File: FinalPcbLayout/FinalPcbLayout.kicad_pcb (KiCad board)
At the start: 4 copper layers, 106.7 x 78.7 mm, 52 parts, among them J1 Conn_02x05_Odd_Even, J2 Conn_01x04_Pin, J3 Serial Out, J4 Conn_01x11_Pin, J5 USB_C_Receptacle, J6 Conn_01x02_Pin, J8 Micro_SD_Card, Q1 NMOS, SW1 SW_Push, U1 ESP32-WROOM-32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

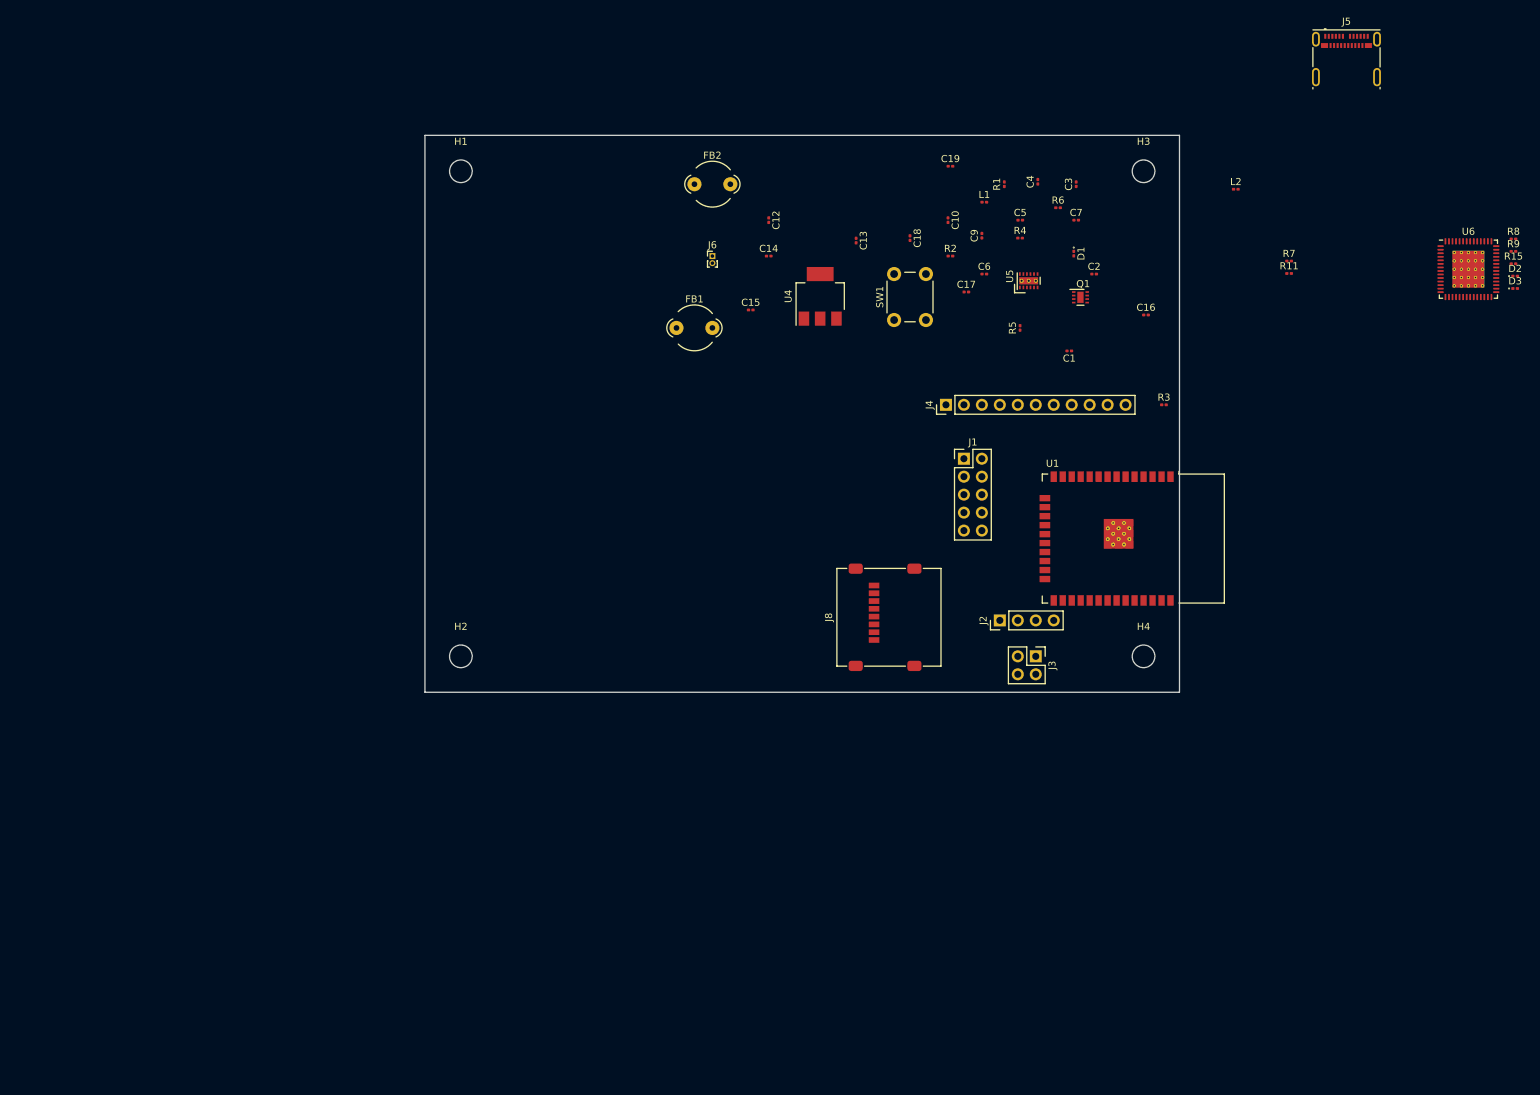
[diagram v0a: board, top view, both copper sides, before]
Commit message: route some gnd
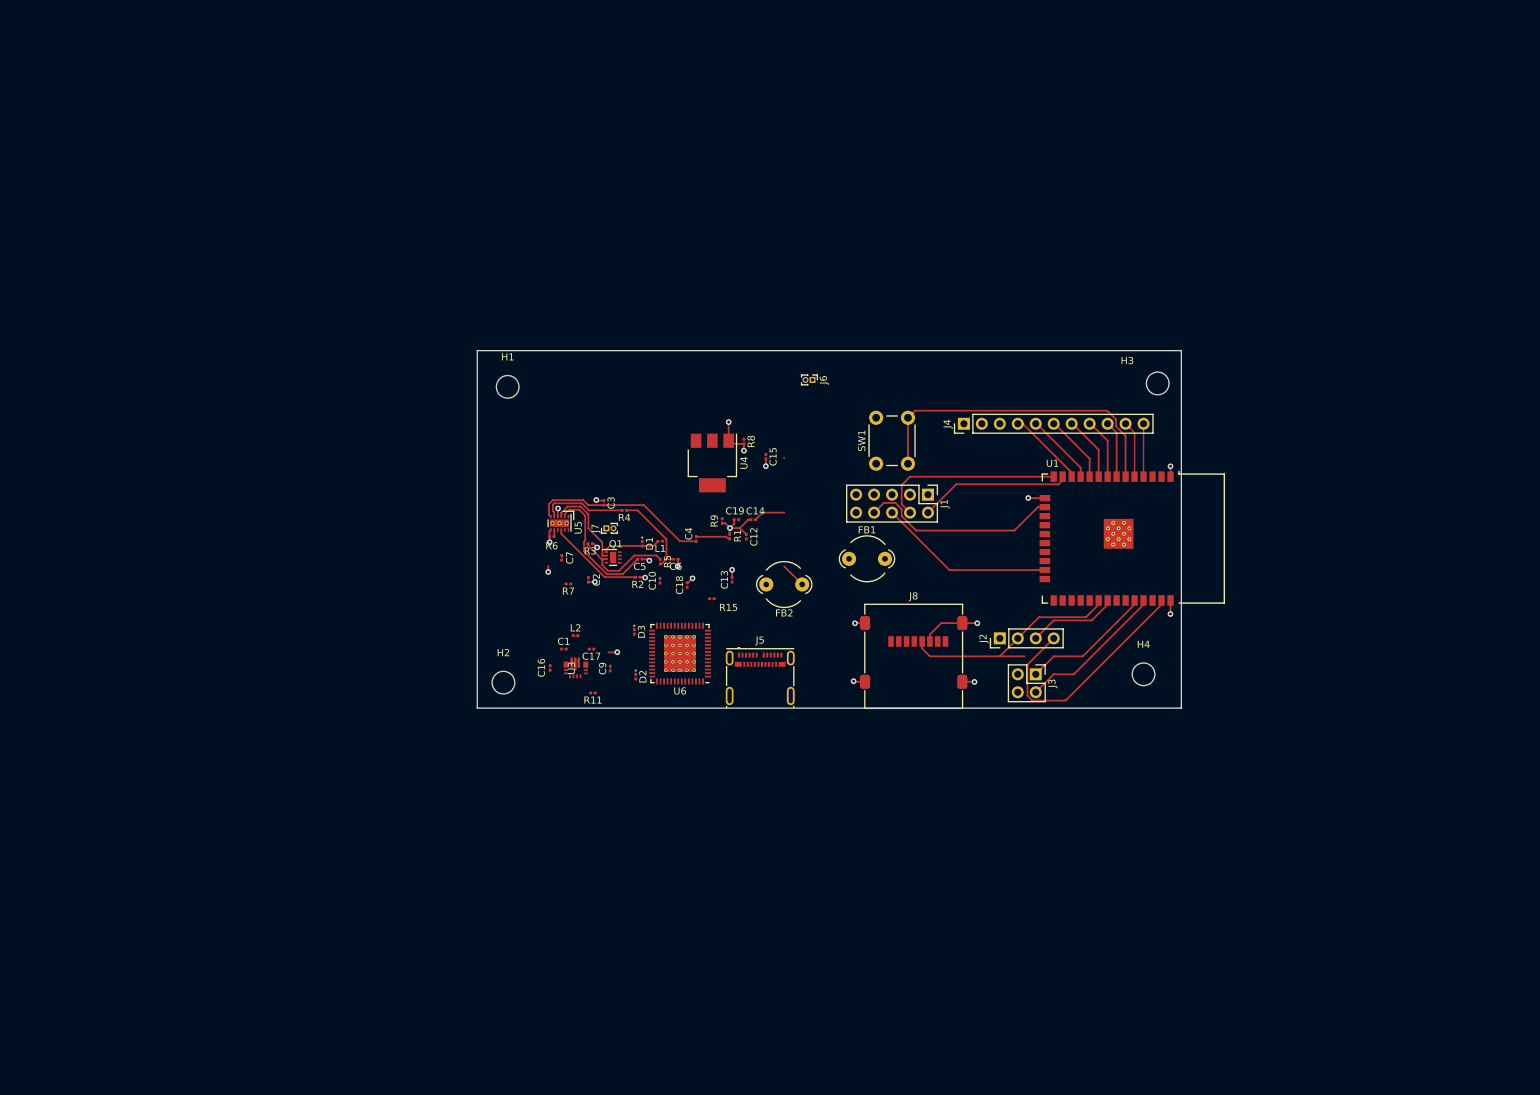
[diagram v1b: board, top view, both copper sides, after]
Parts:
- added J7: Conn_01x02_Pin, Connector_PinHeader_1.00mm:PinHeader_1x02_P1.00mm_Vertical, F.Cu at (101.8, 101.3)
- added U3: ~, OSMI-parts:VQFN-15-1EP-2.5x3mm_P0.5mm, F.Cu at (97.5, 121.0)
- moved D2 136.6 mm to (106.0, 122.3), turned to -90 degrees
- moved D3 133.7 mm to (105.8, 115.9), turned to -90 degrees
- moved U6 124.0 mm to (112.3, 119.0), turned to 180 degrees
- moved R15 122.8 mm to (116.8, 111.2)
- moved J5 120.5 mm to (123.6, 122.4)
- moved R9 118.2 mm to (118.2, 100.2), turned to -90 degrees
- moved R11 114.9 mm to (100.0, 124.5), turned to 180 degrees
- moved L2 112.7 mm to (97.5, 116.5)
- moved R8 112.5 mm to (121.3, 89.0), turned to -90 degrees
- moved R7 111.6 mm to (96.5, 109.1), turned to 180 degrees
- moved C16 97.9 mm to (93.9, 121.0), turned to -90 degrees
- moved C7 87.0 mm to (95.5, 105.5), turned to 90 degrees
- moved R6 85.4 mm to (94.1, 102.5)
- moved C2 83.6 mm to (99.3, 108.6), turned to 90 degrees
- moved R3 83.5 mm to (99.6, 103.5), turned to 180 degrees
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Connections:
- J5 pad A1: /usb/GND1 -> GND
- J5 pad A12: /usb/GND1 -> GND
- J5 pad A5: Net-(J5-CC1) -> /usb/PD1_CC1
- J5 pad A6: /usb/D+1 -> /usb/D+
- J5 pad A7: /usb/D-1 -> /usb/D-
- J5 pad B1: /usb/GND1 -> GND
- J5 pad B12: /usb/GND1 -> GND
- J5 pad B5: Net-(J5-CC2) -> /usb/PD1_CC2
- J5 pad B6: /usb/D-1 -> /usb/D+
- J5 pad B7: /usb/D+1 -> /usb/D-
- U6 pad 11: unconnected-(U6-VCORE-Pad11) -> +1V2
- U6 pad 19: unconnected-(U6-VREGOUT-Pad19) -> +1V2
- U6 pad 22: unconnected-(U6-VCORE-Pad22) -> +1V2
- U6 pad 36: unconnected-(U6-VCORE-Pad36) -> +1V2
- U6 pad 46: unconnected-(U6-VCORE-Pad46) -> +1V2
- U6 pad 52: unconnected-(U6-PD1_CC2-Pad52) -> /usb/PD1_CC2
- U6 pad 55: unconnected-(U6-PD1_CC1-Pad55) -> /usb/PD1_CC1
- U6 pad 56: unconnected-(U6-VCORE-Pad56) -> +1V2
- U6 pad 7: unconnected-(U6-GPIO0-Pad7) -> /usb/I2CSDA
- U6 pad 8: unconnected-(U6-GPIO1-Pad8) -> /usb/I2CSCL
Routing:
- net GND: track 0.00 -> 48.2 mm, vias 0 -> 23
- net /ESTOP: track 0.00 -> 45.5 mm
- net /COPI: track 0.00 -> 35.1 mm
- net /SCLK: track 0.00 -> 33.5 mm
- net /JTAG_TDI: track 0.00 -> 28.3 mm
- net /JTAG_TCK: track 0.00 -> 26.4 mm
- net Net-(U5-COMP): track 0.00 -> 25.3 mm
- net /JTAG_TDO: track 0.00 -> 25.0 mm
- net /JTAG_TMS: track 0.00 -> 21.4 mm
- net Net-(J3-Pin_2): track 0.00 -> 21.0 mm
- net Net-(U5-VCC): track 0.00 -> 18.7 mm
- net Net-(J3-Pin_1): track 0.00 -> 18.6 mm
- net Net-(Q1-S): track 0.00 -> 14.1 mm
- net Net-(U5-RT): track 0.00 -> 13.6 mm
- net /CIPO: track 0.00 -> 12.7 mm
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- added copper zone on In1.Cu, net GND
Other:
- board size 106.7 x 78.7 mm -> 99.5 x 50.5 mm

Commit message: power supplies
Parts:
- removed J1: Conn_02x05_Odd_Even, Connector_PinHeader_2.54mm:PinHeader_2x05_P2.54mm_Vertical
- removed J3: Serial Out, Connector_PinHeader_2.54mm:PinHeader_2x02_P2.54mm_Vertical
- removed R9: 5.1k, Resistor_SMD:R_0201_0603Metric
- added C11: 22uF, Capacitor_SMD:C_0603_1608Metric, F.Cu at (65.3, 105.0)
- added C20: 3.3u, Capacitor_SMD:C_0603_1608Metric, F.Cu at (59.3, 102.5)
- added C8: 1uF, Capacitor_SMD:C_0603_1608Metric, F.Cu at (65.3, 102.5)
- added R10: 523k, Resistor_SMD:R_0603_1608Metric, F.Cu at (137.2, 95.2)
- added R12: 100k, Resistor_SMD:R_0603_1608Metric, F.Cu at (137.2, 96.8)
- added R13: 10k, Resistor_SMD:R_0603_1608Metric, F.Cu at (128.7, 96.6)
- added R14: 10k 1%, Resistor_SMD:R_0603_1608Metric, F.Cu at (59.3, 105.0)
- added R16: 1k, Resistor_SMD:R_0603_1608Metric, F.Cu at (59.3, 107.5)
- added R17: 1k, Resistor_SMD:R_0603_1608Metric, F.Cu at (59.3, 110.0)
- added R18: ???, Resistor_SMD:R_0603_1608Metric, F.Cu at (59.3, 112.5)
- added R19: ???, Resistor_SMD:R_0603_1608Metric, F.Cu at (59.3, 115.0)
- added U2: ~, Package_DFN_QFN:QFN-16-1EP_3x3mm_P0.5mm_EP1.45x1.45mm, F.Cu at (154.8, 100.2)
- C1, C10, C16, C17, C18, C19, C2, C3, C4, C5, C6, C7, C9: footprint Capacitor_SMD:C_0201_0603Metric -> Capacitor_SMD:C_0603_1608Metric
- C12, C13, C14, C15: footprint Resistor_SMD:R_0201_0603Metric -> Capacitor_SMD:C_0603_1608Metric
- D1: footprint Diode_SMD:D_0201_0603Metric -> Diode_SMD:D_0603_1608Metric
- J2: footprint Connector_PinHeader_2.54mm:PinHeader_1x04_P2.54mm_Vertical -> TerminalBlock_TE-Connectivity:TerminalBlock_TE_282834-4_1x04_P2.54mm_Horizontal
- J6: footprint Connector_PinHeader_1.00mm:PinHeader_1x02_P1.00mm_Vertical -> Connector_PinHeader_2.54mm:PinHeader_1x02_P2.54mm_Horizontal
- L1, L2: footprint Inductor_SMD:L_0201_0603Metric -> Inductor_SMD:L_Coilcraft_XAL8050-223
- R1, R11, R15, R2, R3, R4, R5, R6, R7: footprint Resistor_SMD:R_0201_0603Metric -> Resistor_SMD:R_0603_1608Metric
- R8: value 5.1k -> 370k; footprint Resistor_SMD:R_0201_0603Metric -> Resistor_SMD:R_0603_1608Metric
- SW1: footprint Button_Switch_THT:SW_PUSH_6mm -> TerminalBlock_TE-Connectivity:TerminalBlock_TE_282834-2_1x02_P2.54mm_Horizontal
- U4: footprint Package_TO_SOT_SMD:SOT-223-3_TabPin2 -> Package_TO_SOT_SMD:SOT-223
- moved J4 71.9 mm to (86.0, 114.0), turned to 180 degrees
- moved C10 54.1 mm to (112.7, 162.7)
- moved D2 54.1 mm to (109.2, 176.2)
- moved J7 54.1 mm to (105.1, 155.2)
- moved R2 54.1 mm to (109.5, 162.1)
- moved C7 54.1 mm to (98.8, 159.4)
- moved D3 54.1 mm to (109.0, 169.9)
- moved R15 54.1 mm to (120.0, 165.2)
- moved R3 54.1 mm to (102.8, 157.4)
- moved C6 54.1 mm to (114.9, 159.6)
- moved Q1 54.1 mm to (106.0, 159.4)
- moved R5 54.1 mm to (112.7, 159.9)
- moved U6 54.1 mm to (115.5, 172.9)
- moved H2 52.6 mm to (72.4, 173.5)
- moved C9 47.8 mm to (133.8, 157.2)
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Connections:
- R8 pad 1: Net-(J5-CC2) -> +5V
- R8 pad 2: GND -> /SD_MODE
- U1 pad 34: Net-(J3-Pin_1) -> unconnected-(U1-RXD0/IO3-Pad34)
- U1 pad 35: Net-(J3-Pin_2) -> unconnected-(U1-TXD0/IO1-Pad35)
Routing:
- net +3.3V: track 0.00 -> 35.0 mm
- net /ESTOP: track 45.5 -> 13.0 mm, vias 0 -> 1
- net /JTAG_TDI: track 28.3 -> 0.00 mm
- net /IO22: track 0.00 -> 28.2 mm, vias 0 -> 2
- net /IO17: track 0.00 -> 27.9 mm
- net /JTAG_TCK: track 26.4 -> 0.00 mm
- net /JTAG_TDO: track 25.0 -> 0.00 mm
- net /JTAG_TMS: track 21.4 -> 0.00 mm
- net Net-(J3-Pin_2): track 21.0 -> 0.00 mm
- net /COPI: track 35.1 -> 14.7 mm, vias 0 -> 1
- net Net-(U5-COMP): track 25.3 -> 5.75 mm
- net Net-(J3-Pin_1): track 18.6 -> 0.00 mm
- net GND: track 48.2 -> 30.2 mm, vias 23 -> 22
- net /SCLK: track 33.5 -> 49.8 mm
- net Net-(U3-L2): track 0.00 -> 16.0 mm, vias 0 -> 11
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- added copper zone on F.Cu, net +5V
- added copper zone on In2.Cu, net +5V
- added copper zone on F.Cu, net /Power/USB_Vin
- added copper zone on F.Cu, net GND
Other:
- board size 99.5 x 50.5 mm -> 99.5 x 46.2 mm

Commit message: pOWER DONE
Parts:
- removed J7: Conn_01x02_Pin, Connector_PinHeader_1.00mm:PinHeader_1x02_P1.00mm_Vertical
- C5: value C -> 1uF
- D1: footprint Diode_SMD:D_0603_1608Metric -> SL42_E3_57T:CR_2-E3&slash_57T_VIS
- moved C10 93.4 mm to (168.8, 88.0), turned to 0 degrees
- moved C20 75.2 mm to (132.3, 120.6)
- moved R14 75.2 mm to (132.3, 123.1)
- moved R16 75.2 mm to (132.3, 125.6)
- moved R17 75.2 mm to (132.3, 128.1)
- moved R18 75.2 mm to (132.3, 130.6)
- moved R19 75.2 mm to (132.3, 133.1)
- moved C11 75.2 mm to (138.3, 123.1)
- moved R2 69.1 mm to (102.5, 93.4), turned to -90 degrees
- moved D2 64.4 mm to (127.1, 114.4)
- moved D3 64.4 mm to (126.9, 108.0)
- moved U6 64.4 mm to (133.4, 111.1)
- moved R15 58.5 mm to (141.1, 110.6)
- moved C9 54.2 mm to (96.2, 118.0), turned to 180 degrees
- moved C6 52.9 mm to (108.4, 107.1)
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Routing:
- net +5V: track 14.6 -> 36.4 mm
- net Net-(Q1-G): track 0.00 -> 20.2 mm, vias 0 -> 2
- net Net-(D1-A): track 0.00 -> 12.3 mm
- net +12V: track 0.00 -> 11.3 mm, vias 0 -> 2
- net Net-(U5-CS): track 0.00 -> 10.6 mm
- net Net-(Q1-S): track 0.00 -> 10.0 mm
- net GND: track 30.2 -> 36.7 mm, vias 22 -> 29
- net Net-(U5-RT): track 0.00 -> 2.46 mm
- net Net-(U5-SS): track 0.00 -> 2.30 mm
- net Net-(C6-Pad2): track 1.19 -> 2.98 mm
- added copper zone on F.Cu, net +12V

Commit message: Tyra's work is done here
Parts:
- removed C20: 3.3u, Capacitor_SMD:C_0603_1608Metric
- removed D2, D3: LED, LED_SMD:LED_0201_0603Metric
- removed J5: USB_C_Receptacle, Connector_USB:USB_C_Receptacle_Molex_105450-0101
- removed R14, R15: 10k 1%, Resistor_SMD:R_0603_1608Metric
- removed R16, R17: 1k, Resistor_SMD:R_0603_1608Metric
- removed R18, R19: ???, Resistor_SMD:R_0603_1608Metric
- removed U6: ~, Package_DFN_QFN:QFN-56-1EP_8x8mm_P0.5mm_EP4.5x5.2mm_ThermalVias
- moved C11 40.8 mm to (163.1, 90.7), turned to 180 degrees
- moved J4 1.50 mm to (84.2, 116.4)
- moved H3 1.40 mm to (179.3, 83.4)
- moved SW1 1.30 mm to (173.4, 83.5)
- moved C14 0.52 mm to (158.6, 116.0)
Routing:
- net /IO33: track 0.00 -> 102.8 mm, vias 0 -> 1
- net /IO35: track 0.00 -> 102.5 mm, vias 0 -> 2
- net /IO25: track 0.00 -> 102.2 mm, vias 0 -> 1
- net /IO27: track 0.00 -> 102.0 mm, vias 0 -> 2
- net /IO26: track 0.00 -> 101.1 mm, vias 0 -> 2
- net /Sense_VN: track 0.00 -> 100.9 mm, vias 0 -> 2
- net /IO32: track 0.00 -> 98.0 mm, vias 0 -> 2
- net /Sense_VP: track 0.00 -> 97.3 mm, vias 0 -> 2
- net +3.3V: track 35.0 -> 123.5 mm, vias 0 -> 1
- net +12V: track 11.3 -> 40.5 mm
- net /IO21: track 0.00 -> 25.2 mm, vias 0 -> 2
- net +5V: track 36.4 -> 49.9 mm
- net GND: track 36.7 -> 47.0 mm, vias 29 -> 33
- net Net-(U3-L2): track 16.0 -> 14.2 mm, vias 11 -> 7
- net Net-(Q1-G): track 20.2 -> 21.8 mm
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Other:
- board size 99.5 x 46.2 mm -> 100.9 x 46.7 mm

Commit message: Cool
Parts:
- C1, C2, C3, C8: footprint Capacitor_SMD:C_0603_1608Metric -> Capacitor_SMD:C_0402_1005Metric
- C10, C19, C6, C9: footprint Capacitor_SMD:C_0603_1608Metric -> Capacitor_SMD:C_0805_2012Metric
- C4: footprint Capacitor_SMD:C_0603_1608Metric -> Capacitor_SMD:C_1812_4532Metric
- R3, R4: footprint Resistor_SMD:R_0603_1608Metric -> Resistor_SMD:R_1206_3216Metric
- moved R1 4.89 mm to (110.9, 105.0)
- moved C3 3.32 mm to (110.2, 102.5)
- moved R4 2.01 mm to (104.5, 110.5)
- moved C17 1.70 mm to (131.6, 99.2)
- moved C18 1.70 mm to (136.2, 91.9)
- moved R10 1.70 mm to (135.3, 95.2)
- moved R11 1.70 mm to (135.3, 98.4)
- moved U3 1.70 mm to (130.6, 96.2)
- moved C16 1.70 mm to (125.3, 92.2)
- moved R13 1.70 mm to (126.8, 96.6)
- moved C19 1.70 mm to (139.3, 91.9)
- moved L2 1.70 mm to (130.4, 85.1)
- moved R12 1.70 mm to (135.3, 96.8)
- moved C4 1.55 mm to (106.4, 101.9)
- moved R3 0.99 mm to (111.7, 108.5)
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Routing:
- net Net-(C4-Pad1): track 1.72 -> 4.18 mm
- net Net-(U5-CS): track 10.6 -> 12.8 mm
- net Net-(C6-Pad2): track 2.98 -> 4.88 mm
- net Net-(Q1-S): track 9.54 -> 11.1 mm
- net /IO35: track 102.5 -> 101.0 mm
- net Net-(U5-COMP): track 5.75 -> 6.99 mm
- net GND: track 47.0 -> 47.4 mm, vias 33 -> 36
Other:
- board size 100.9 x 46.7 mm -> 100.9 x 47.2 mm
- board text added: "ECE TEAM 11 OSMI SYRINGE PUMP"

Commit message: Part Finalization
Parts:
- added C20: 3.3u, Capacitor_SMD:C_0603_1608Metric, F.Cu at (138.1, 105.0)
- added D2: LED, LED_SMD:LED_0201_0603Metric, F.Cu at (117.6, 113.2)
- added D3: LED, LED_SMD:LED_0201_0603Metric, F.Cu at (116.8, 113.2)
- added J1: Conn_02x05_Odd_Even, Connector_PinHeader_2.54mm:PinHeader_2x05_P2.54mm_Vertical, F.Cu at (121.9, 155.2)
- added J3: Barrel_Jack, Connector_BarrelJack:BarrelJack_GCT_DCJ200-10-A_Horizontal, F.Cu at (125.1, 136.1)
- added J5: USB_C_Receptacle, Connector_USB:USB_C_Receptacle_Molex_105450-0101, F.Cu at (124.7, 121.9)
- added R14: 10k 1%, Resistor_SMD:R_0603_1608Metric, F.Cu at (138.1, 107.5)
- added R15: 10k 1%, Resistor_SMD:R_0603_1608Metric, F.Cu at (138.1, 110.0)
- added R16: 1k, Resistor_SMD:R_0603_1608Metric, F.Cu at (138.1, 112.5)
- added R17: 1k, Resistor_SMD:R_0603_1608Metric, F.Cu at (138.1, 115.0)
- added R18: ???, Resistor_SMD:R_0603_1608Metric, F.Cu at (138.1, 117.5)
- added R19: ???, Resistor_SMD:R_0603_1608Metric, F.Cu at (138.1, 120.0)
- added U6: ~, Package_DFN_QFN:QFN-56-1EP_8x8mm_P0.5mm_EP4.5x5.2mm_ThermalVias, F.Cu at (124.7, 111.8)
- C1, C2, C3, C8: footprint Capacitor_SMD:C_0402_1005Metric -> Capacitor_SMD:C_0603_1608Metric
- C10, C19, C6, C9: footprint Capacitor_SMD:C_0805_2012Metric -> Capacitor_SMD:C_0603_1608Metric
- R3, R4: footprint Resistor_SMD:R_1206_3216Metric -> Resistor_SMD:R_0603_1608Metric
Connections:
- C1 pad 2: +5V -> /Power/V_in
- C16 pad 1: /Power/USB_Vin -> /Power/V_in
- C9 pad 2: +5V -> /Power/V_in
- L1 pad 1: +5V -> /Power/V_in
- R13 pad 1: /Power/USB_Vin -> /Power/V_in
- U3 pad 1: /Power/USB_Vin -> /Power/V_in
- U3 pad 12: /Power/USB_Vin -> /Power/V_in
- U3 pad 13: /Power/USB_Vin -> /Power/V_in
- U5 pad 1: +5V -> /Power/V_in
- U5 pad 12: +5V -> /Power/V_in
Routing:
- net /Power/V_in: track 0.00 -> 14.4 mm
- net /Power/USB_Vin: track 14.4 -> 0.00 mm
- net +3.3V: track 123.5 -> 130.2 mm
- net GND: track 47.4 -> 53.2 mm
- net /usb/RXLED: track 0.00 -> 4.66 mm
- net /usb/TXLED: track 0.00 -> 3.34 mm
- net /usb/D+: track 0.00 -> 1.61 mm, vias 0 -> 2
- net /usb/D-: track 0.00 -> 1.61 mm
- net +3V3: track 0.00 -> 1.41 mm, vias 0 -> 1
- net Net-(J5-VBUS-PadA4): track 0.00 -> 1.27 mm
- added copper zone on F.Cu, net (none)
- removed copper zone on F.Cu, net /Power/USB_Vin
